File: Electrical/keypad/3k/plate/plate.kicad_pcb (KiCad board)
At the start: 2 copper layers, 68 x 68 mm, 8 parts

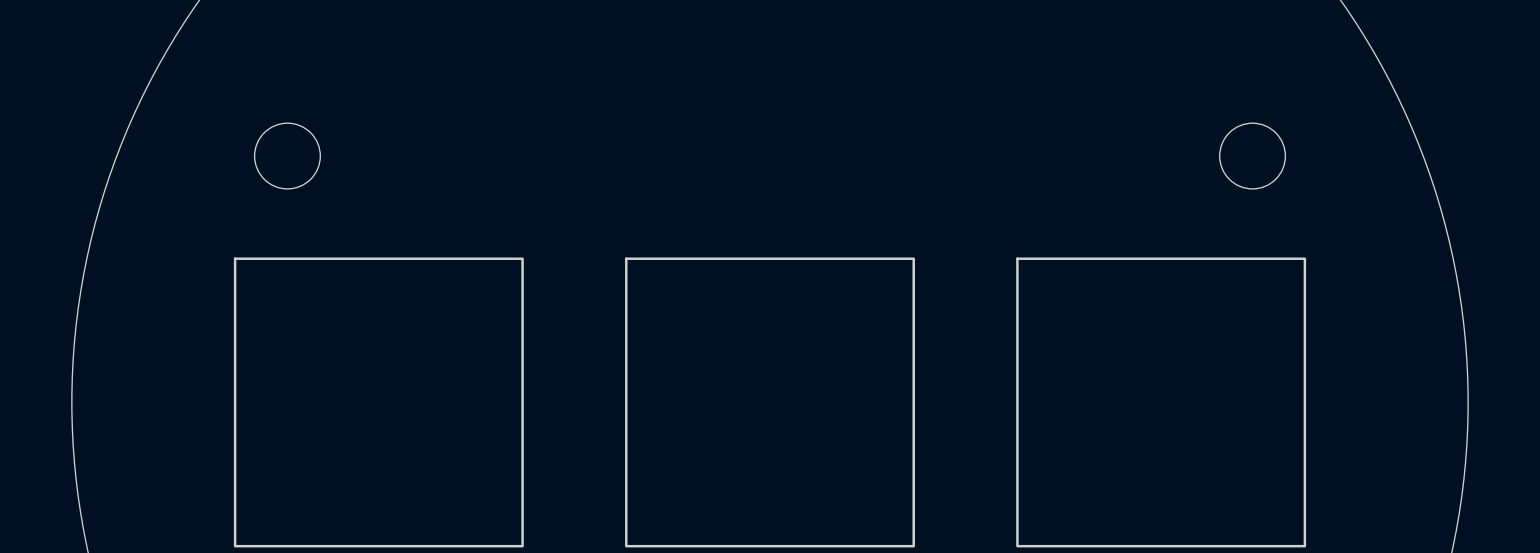
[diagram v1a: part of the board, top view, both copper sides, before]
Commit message: update plate holes
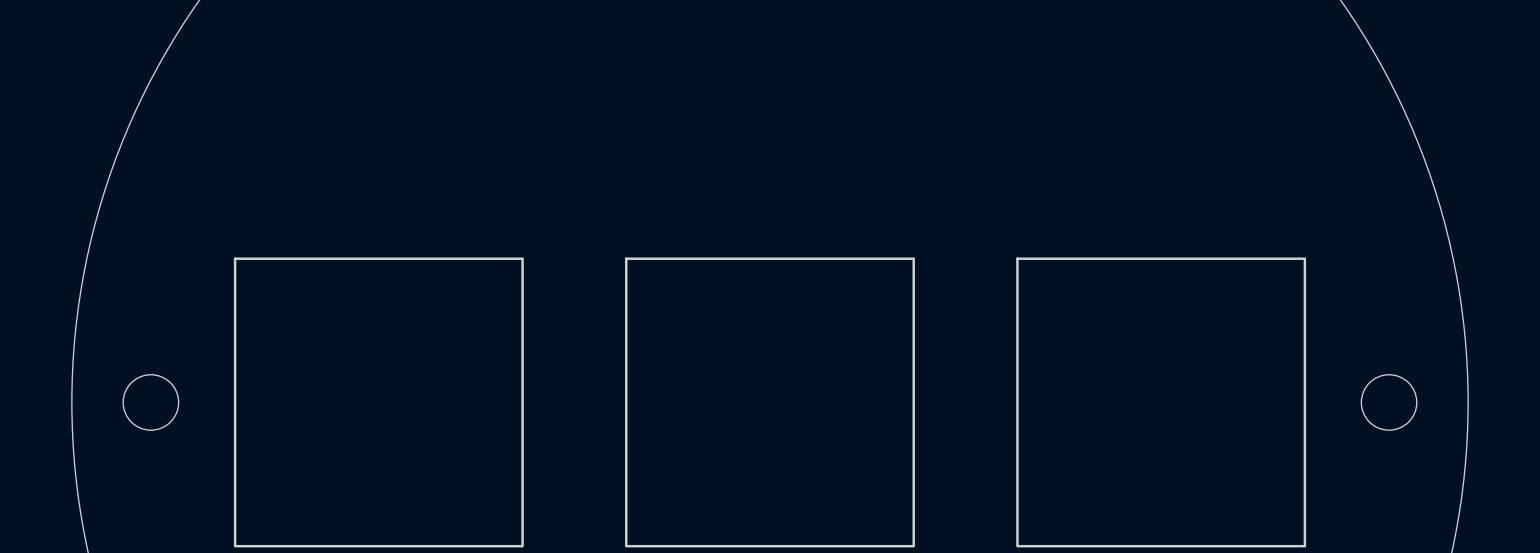
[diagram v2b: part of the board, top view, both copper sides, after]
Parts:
- removed H1, H2: MountingHole_3.2mm_M3, MountingHole:MountingHole_3.2mm_M3
- added REF**: MountingHole_2.7mm_M2.5, MountingHole:MountingHole_2.7mm_M2.5, F.Cu at (130.2, 100.0)
- added REF**: MountingHole_2.7mm_M2.5, MountingHole:MountingHole_2.7mm_M2.5, F.Cu at (69.8, 100.0)
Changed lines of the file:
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@@
     (pad "" np_thru_hole circle (at 0 0) (size 2.7 2.7) (drill 2.7) (layers "*.Cu" "*.Mask"))
+  )
+  (footprint "MountingHole:MountingHole_2.7mm_M2.5" (layer "F.Cu")
+    (at 130.15 100)
+    (descr "Mounting Hole 2.7mm, no annular, M2.5")
+    (tags "mounting hole 2.7mm no annular m2.5")
+    (attr exclude_from_pos_files exclude_from_bom)
+    (fp_text reference "REF**" (at 0 -3.7) (layer "F.SilkS") hide
+        (effects (font (size 1 1) (thickness 0.15)))
+    )
+    (fp_text value "MountingHole_2.7mm_M2.5" (at 0 3.7) (layer "F.Fab")
+        (effects (font (size 1 1) (thickness 0.15)))
+    )
+    (fp_text user "${REFERENCE}" (at 0 0) (layer "F.Fab")
+        (effects (font (size 1 1) (thickness 0.15)))
+    )
+    (fp_circle (center 0 0) (end 2.7 0)
+      (stroke (width 0.15) (type solid)) (fill none) (layer "Cmts.User"))
+    (fp_circle (center 0 0) (end 2.95 0)
+      (stroke (width 0.05) (type solid)) (fill none) (layer "F.CrtYd"))
+    (pad "" np_thru_hole circle (at 0 0) (size 2.7 2.7) (drill 2.7) (layers "*.Cu" "*.Mask"))
+  )
+  (footprint "MountingHole:MountingHole_2.7mm_M2.5" (layer "F.Cu")
+    (at 69.85 100)
+    (descr "Mounting Hole 2.7mm, no annular, M2.5")
+    (tags "mounting hole 2.7mm no annular m2.5")
+    (attr exclude_from_pos_files exclude_from_bom)
+    (fp_text reference "REF**" (at 0 -3.7) (layer "F.SilkS") hide
+        (effects (font (size 1 1) (thickness 0.15)))
+    )
+    (fp_text value "MountingHole_2.7mm_M2.5" (at 0 3.7) (layer "F.Fab")
+        (effects (font (size 1 1) (thickness 0.15)))
+    )
+    (fp_text user "${REFERENCE}" (at 0 0) (layer "F.Fab")
+        (effects (font (size 1 1) (thickness 0.15)))
+    )
+    (fp_circle (center 0 0) (end 2.7 0)
+      (stroke (width 0.15) (type solid)) (fill none) (layer "Cmts.User"))
+    (fp_circle (center 0 0) (end 2.95 0)
+      (stroke (width 0.05) (type solid)) (fill none) (layer "F.CrtYd"))
+    (pad "" np_thru_hole circle (at 0 0) (size 2.7 2.7) (drill 2.7) (layers "F&B.Cu" "*.Mask"))
   )
   (footprint "Button_Switch_Keyboard:SW_Lekker_1.00u_Plate" (layer "F.Cu")
@@
     (pad "" np_thru_hole circle (at 0 0) (size 2.8 2.8) (drill 2.8) (layers "F&B.Cu" "*.Mask"))
   )
-  (footprint "MountingHole:MountingHole_3.2mm_M3" (layer "B.Cu")
-    (at 123.5 88 180)
-    (descr "Mounting Hole 3.2mm, no annular, M3")
-    (tags "mounting hole 3.2mm no annular m3")
-    (property "Sheetfile" "RP2040_minimal.kicad_sch")
-    (property "Sheetname" "")
-    (property "ki_description" "Mounting Hole with connection")
-    (property "ki_keywords" "mounting hole")
-    (attr exclude_from_pos_files exclude_from_bom)
-    (fp_text reference "H2" (at 0 4.2) (layer "B.SilkS") hide
-        (effects (font (size 1 1) (thickness 0.15)) (justify mirror))
-    )
-    (fp_text value "MountingHole_3.2mm_M3" (at 0 -4.2) (layer "B.Fab")
-        (effects (font (size 1 1) (thickness 0.15)) (justify mirror))
-    )
-    (fp_text user "${REFERENCE}" (at 0 0) (layer "B.Fab")
-        (effects (font (size 1 1) (thickness 0.15)) (justify mirror))
-    )
-    (fp_circle (center 0 0) (end 3.2 0)
-      (stroke (width 0.15) (type solid)) (fill none) (layer "Cmts.User"))
-    (fp_circle (center 0 0) (end 3.45 0)
-      (stroke (width 0.05) (type solid)) (fill none) (layer "B.CrtYd"))
-    (pad "" np_thru_hole circle (at 0 0 180) (size 3.2 3.2) (drill 3.2) (layers "*.Cu" "*.Mask"))
-  )
-  (footprint "MountingHole:MountingHole_3.2mm_M3" (layer "B.Cu")
-    (at 76.5 88 180)
-    (descr "Mounting Hole 3.2mm, no annular, M3")
-    (tags "mounting hole 3.2mm no annular m3")
-    (property "Sheetfile" "RP2040_minimal.kicad_sch")
-    (property "Sheetname" "")
-    (property "ki_description" "Mounting Hole with connection")
-    (property "ki_keywords" "mounting hole")
-    (attr exclude_from_pos_files exclude_from_bom)
-    (fp_text reference "H1" (at 0 4.2) (layer "B.SilkS") hide
-        (effects (font (size 1 1) (thickness 0.15)) (justify mirror))
-    )
-    (fp_text value "MountingHole_3.2mm_M3" (at 0 -4.2) (layer "B.Fab")
-        (effects (font (size 1 1) (thickness 0.15)) (justify mirror))
-    )
-    (fp_text user "${REFERENCE}" (at 0 0) (layer "B.Fab")
-        (effects (font (size 1 1) (thickness 0.15)) (justify mirror))
-    )
-    (fp_circle (center 0 0) (end 3.2 0)
-      (stroke (width 0.15) (type solid)) (fill none) (layer "Cmts.User"))
-    (fp_circle (center 0 0) (end 3.45 0)
-      (stroke (width 0.05) (type solid)) (fill none) (layer "B.CrtYd"))
-    (pad "" np_thru_hole circle (at 0 0 180) (size 3.2 3.2) (drill 3.2) (layers "*.Cu" "*.Mask"))
-  )
   (gr_circle (center 100 100) (end 134 100)
     (stroke (width 0.05) (type default)) (fill none) (layer "Edge.Cuts"))
@@
     (polygon
       (pts
-        (xy 22.495944 41.412769)
-        (xy 26.657626 34.240505)
-        (xy 30.78815 41.430759)
-      )
-    )
-  )
-  (zone (net 0) (net_name "") (layers "F&B.Cu") (hatch edge 0.5)
-    (connect_pads (clearance 0))
-    (min_thickness 0.25) (filled_areas_thickness no)
-    (keepout (tracks not_allowed) (vias not_allowed) (pads not_allowed) (copperpour not_allowed) (footprints allowed))
-    (fill (thermal_gap 0.5) (thermal_bridge_width 0.5))
-    (polygon
-      (pts
         (xy 76.134738 111.404872)
         (xy 74.053897 114.991005)
@@
     (polygon
       (pts
-        (xy 44.015589 42.16402)
-        (xy 52.338953 27.819492)
-        (xy 60.6 42.2)
-      )
-    )
-  )
-  (zone (net 0) (net_name "") (layers "F&B.Cu") (hatch edge 0.5)
-    (connect_pads (clearance 0))
-    (min_thickness 0.25) (filled_areas_thickness no)
-    (keepout (tracks not_allowed) (vias not_allowed) (pads not_allowed) (copperpour not_allowed) (footprints allowed))
-    (fill (thermal_gap 0.5) (thermal_bridge_width 0.5))
-    (polygon
-      (pts
         (xy 86.834738 86.854872)
         (xy 84.753897 90.441005)
@@
     (polygon
       (pts
-        (xy 21.372114 56.890007)
-        (xy 27.614637 46.13161)
-        (xy 33.810423 56.916992)
-      )
-    )
-  )
-  (zone (net 0) (net_name "") (layers "F&B.Cu") (hatch edge 0.5)
-    (connect_pads (clearance 0))
-    (min_thickness 0.25) (filled_areas_thickness no)
-    (keepout (tracks not_allowed) (vias not_allowed) (pads not_allowed) (copperpour not_allowed) (footprints allowed))
-    (fill (thermal_gap 0.5) (thermal_bridge_width 0.5))
-    (polygon
-      (pts
-        (xy 12.695944 57.012769)
-        (xy 16.857626 49.840505)
-        (xy 20.98815 57.030759)
-      )
-    )
-  )
-  (zone (net 0) (net_name "") (layers "F&B.Cu") (hatch edge 0.5)
-    (connect_pads (clearance 0))
-    (min_thickness 0.25) (filled_areas_thickness no)
-    (keepout (tracks not_allowed) (vias not_allowed) (pads not_allowed) (copperpour not_allowed) (footprints allowed))
-    (fill (thermal_gap 0.5) (thermal_bridge_width 0.5))
-    (polygon
-      (pts
         (xy 186.759738 50.129872)
         (xy 184.678897 53.716005)
@@
     (polygon
       (pts
-        (xy 34.215589 57.76402)
-        (xy 42.538953 43.419492)
-        (xy 50.8 57.8)
-      )
-    )
-  )
-  (zone (net 0) (net_name "") (layers "F&B.Cu") (hatch edge 0.5)
-    (connect_pads (clearance 0))
-    (min_thickness 0.25) (filled_areas_thickness no)
-    (keepout (tracks not_allowed) (vias not_allowed) (pads not_allowed) (copperpour not_allowed) (footprints allowed))
-    (fill (thermal_gap 0.5) (thermal_bridge_width 0.5))
-    (polygon
-      (pts
         (xy 129.74 95.5)
         (xy 127.659159 99.086133)
@@
     (polygon
       (pts
-        (xy 31.172114 41.290007)
-        (xy 37.414637 30.53161)
-        (xy 43.610423 41.316992)
-      )
-    )
-  )
-  (zone (net 0) (net_name "") (layers "F&B.Cu") (hatch edge 0.5)
-    (connect_pads (clearance 0))
-    (min_thickness 0.25) (filled_areas_thickness no)
-    (keepout (tracks not_allowed) (vias not_allowed) (pads not_allowed) (copperpour not_allowed) (footprints allowed))
-    (fill (thermal_gap 0.5) (thermal_bridge_width 0.5))
-    (polygon
-      (pts
         (xy 88.964738 108.084872)
         (xy 86.883897 111.671005)
@@
     (polygon
       (pts
-        (xy 86.215589 42.96402)
-        (xy 94.538953 28.619492)
-        (xy 102.8 43)
-      )
-    )
-  )
-  (zone (net 0) (net_name "") (layers "F&B.Cu") (hatch edge 0.5)
-    (connect_pads (clearance 0))
-    (min_thickness 0.25) (filled_areas_thickness no)
-    (keepout (tracks not_allowed) (vias not_allowed) (pads not_allowed) (copperpour not_allowed) (footprints allowed))
-    (fill (thermal_gap 0.5) (thermal_bridge_width 0.5))
-    (polygon
-      (pts
         (xy 174.959738 55.529872)
         (xy 172.878897 59.116005)
@@
       )
     )
-  )
-  (zone (net 0) (net_name "") (layers "F&B.Cu") (hatch edge 0.5)
-    (connect_pads (clearance 0))
-    (min_thickness 0.25) (filled_areas_thickness no)
-    (keepout (tracks not_allowed) (vias not_allowed) (pads not_allowed) (copperpour not_allowed) (footprints allowed))
-    (fill (thermal_gap 0.5) (thermal_bridge_width 0.5))
-    (polygon
-      (pts
-        (xy 112.314488 43.849502)
-        (xy 118.557011 33.091105)
-        (xy 124.752797 43.876487)
-      )
-    )
